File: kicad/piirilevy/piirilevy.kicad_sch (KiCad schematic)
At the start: 57 parts, among them SW1 SW_SPST, SW2 SW_Push, SW3 SW_Push, SW4 SW_Push, U1 LM324, U2 LM324, U3 LM324, U4 MAX5033B, U5 LM324, U6 uA7805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

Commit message: ...
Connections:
- net VAHVISTIN_LÄHTÖ: now also U5.13 (-), U5.14; no longer U5.1, U5.2 (-)
- net at R13.2, R14.1: now also U3.8; no longer U3.1
- net at R13.1, R8.1: now also U3.9 (-); no longer U3.2 (-)
- net at R11.2, R9.2: now also U3.10 (+); no longer U3.3 (+)
- net at R6.1: now also U2.6 (-); no longer U2.2 (-)
- net at R6.2, R7.1, R9.1: now also U2.7; no longer U2.1
- net at C4.1, R15.2: now also U5.12 (+); no longer U5.3 (+)
- net at R2.1, TH1.1: now also U2.5 (+); no longer U2.3 (+)
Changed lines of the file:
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@@
     )
   )
-  (symbol (lib_id "Amplifier_Operational:LM324") (at 73.66 74.93 0) (mirror x) (unit 1)
+  (symbol (lib_id "Amplifier_Operational:LM324") (at 73.66 74.93 0) (mirror x) (unit 3)
     (in_bom yes) (on_board yes)
     (property "Reference" "U3" (id 0) (at 73.66 80.01 0))
@@
       (effects (font (size 1.27 1.27)) hide)
     )
-    (pin "1")
-    (pin "2")
-    (pin "3")
+    (pin "10")
+    (pin "8")
+    (pin "9")
   )
   (symbol (lib_id "power:VCC") (at 194.31 111.76 0) (unit 1)
@@
     (pin "2")
   )
-  (symbol (lib_id "Amplifier_Operational:LM324") (at 111.76 72.39 0) (mirror x) (unit 1)
+  (symbol (lib_id "Amplifier_Operational:LM324") (at 111.76 72.39 0) (mirror x) (unit 4)
     (in_bom yes) (on_board yes)
     (property "Reference" "U5" (id 0) (at 111.76 77.47 0))
@@
       (effects (font (size 1.27 1.27)) hide)
     )
-    (pin "1")
-    (pin "2")
-    (pin "3")
+    (pin "12")
+    (pin "13")
+    (pin "14")
   )
   (symbol (lib_id "power:GND") (at 110.49 187.96 0) (unit 1)
@@
     (pin "1")
   )
-  (symbol (lib_id "Amplifier_Operational:LM324") (at 45.72 85.09 0) (unit 1)
+  (symbol (lib_id "Amplifier_Operational:LM324") (at 45.72 85.09 0) (unit 2)
     (in_bom yes) (on_board yes)
     (property "Reference" "U2" (id 0) (at 45.72 75.7682 0))
@@
       (effects (font (size 1.27 1.27)) hide)
     )
-    (pin "1")
-    (pin "2")
-    (pin "3")
+    (pin "5")
+    (pin "6")
+    (pin "7")
   )
   (symbol (lib_id "Device:C") (at 127 158.75 270) (unit 1)
@@
     )
     (path "/de0d0b26-5dbb-4b0b-8931-3a9405d7e432"
-      (reference "U2") (unit 1) (value "LM324") (footprint "")
+      (reference "U2") (unit 2) (value "LM324") (footprint "")
     )
     (path "/0345509e-dbff-4fb5-9059-bc7781b5488b"
-      (reference "U3") (unit 1) (value "LM324") (footprint "")
+      (reference "U3") (unit 3) (value "LM324") (footprint "")
     )
     (path "/b456cffc-d9d7-4c91-91f2-36ec9a65dd1b"
@@
     )
     (path "/d674ea40-4701-4f3e-93d0-02b0a7afdc20"
-      (reference "U5") (unit 1) (value "LM324") (footprint "")
+      (reference "U5") (unit 4) (value "LM324") (footprint "")
     )
     (path "/b3ed1808-38b3-403b-99a9-68a2b023b131"

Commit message: Muutokset piirilevyyn.
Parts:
- added C18: 22u, Capacitor_THT:C_Radial_D5.0mm_H7.0mm_P2.00mm, symbol Device:C
- added R20, R21: 4.7K, Resistor_THT:R_Axial_DIN0204_L3.6mm_D1.6mm_P7.62mm_Horizontal, symbol Device:R
- C1, C12, C13, C9: footprint (none) -> Capacitor_THT:C_Radial_D5.0mm_H7.0mm_P2.00mm
- C10, C11, C2, C3, C4, C5, C7, C8: footprint (none) -> Capacitor_THT:C_Disc_D4.3mm_W1.9mm_P5.00mm
- C14: footprint (none) -> Capacitor_THT:C_Radial_D4.0mm_H5.0mm_P1.50mm
- C15, C16, C17: footprint (none) -> Capacitor_THT:C_Rect_L7.0mm_W2.5mm_P5.00mm
- C6: footprint (none) -> Capacitor_THT:C_Radial_D10.0mm_H16.0mm_P5.00mm
- L1: footprint (none) -> Inductor_THT:L_Radial_D8.7mm_P5.00mm_Fastron_07HCP
- RV1: footprint (none) -> Potentiometer_THT:Potentiometer_ACP_CA9-H3,8_Horizontal
- TH1, V1: footprint (none) -> Connector_PinHeader_2.00mm:PinHeader_1x02_P2.00mm_Vertical
- U1: renamed from U3; footprint (none) -> Package_DIP:DIP-14_W7.62mm_LongPads
- U1: footprint Package_DIP:DIP-14_W10.16mm_LongPads -> Package_DIP:DIP-14_W7.62mm_LongPads
- U1: renamed from U5; footprint (none) -> Package_DIP:DIP-14_W7.62mm_LongPads
- U1: renamed from U2; footprint (none) -> Package_DIP:DIP-14_W7.62mm_LongPads
- U2: renamed from U6; footprint (none) -> Package_TO_SOT_THT:TO-220-3_Horizontal_TabDown
- Y1: footprint (none) -> Crystal:Crystal_HC18-U_Vertical
- renumbered U8 to U3, U7 to U5, U9 to U6
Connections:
- net GND: now also C18.1
- net I2C_SCL: now also R20.2
- net I2C_SDA: now also R21.1
- net LCD_AN: now also DS1.11 (LED(+)); no longer DS1.15 (LED(+))
- net LCD_D4: now also DS1.7 (D4); no longer DS1.11 (D4)
- net LCD_D5: now also DS1.8 (D5); no longer DS1.12 (D5)
- net LCD_D6: now also DS1.9 (D6); no longer DS1.13 (D6)
- net LCD_D7: now also DS1.10 (D7); no longer DS1.14 (D7)
- net VAHVISTIN_LÄHTÖ: now also U1.8, U1.9 (-); no longer U1.13 (-), U1.14
- net VCC: now also C18.2, R20.1, R21.2
- net at R11.2, R9.2: now also U1.5 (+); no longer U1.10 (+)
- net at R13.2, R14.1: now also U1.7; no longer U1.8
- net at R13.1, R8.1: now also U1.6 (-); no longer U1.9 (-)
- net at R19.2: now also DS1.12 (LED(-)); no longer DS1.16 (LED(-))
- net at R6.1: now also U1.13 (-); no longer U1.6 (-)
- net at R6.2, R7.1, R9.1: now also U1.14; no longer U1.7
- net at C4.1, R15.2: now also U1.10 (+); no longer U1.12 (+)
- net at R2.1, TH1.1: now also U1.12 (+); no longer U1.5 (+)

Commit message: kicad muutokset
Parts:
- added D2: 1N4148, Diode_THT:D_DO-35_SOD27_P7.62mm_Horizontal, symbol Diode:1N4148
- added J1: AVR-ISP, Connector_PinHeader_2.54mm:PinHeader_2x03_P2.54mm_Vertical, symbol Connector:AVR-ISP-6
- BZ1, SW1, SW2, SW3, SW4, TH1: footprint Connector_PinHeader_2.00mm:PinHeader_1x02_P2.00mm_Vertical -> Connector_PinHeader_2.54mm:PinHeader_1x02_P2.54mm_Vertical
- DS1: footprint Connector_PinHeader_2.00mm:PinHeader_1x12_P2.00mm_Vertical -> Connector_PinHeader_2.54mm:PinHeader_1x12_P2.54mm_Vertical
- RV1: footprint Potentiometer_THT:Potentiometer_ACP_CA9-H3,8_Horizontal -> Potentiometer_THT:Potentiometer_ACP_CA6-H2,5_Horizontal
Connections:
- net GND: now also J1.6 (GND)
- net SPI_MISO: now also J1.1 (MISO)
- net SPI_MOSI: now also J1.4 (MOSI)
- net SPI_SCK: now also J1.3 (SCK)
- net VCC: now also D2.2 (A); no longer U3.7 (VCC)
- net SW_3 renamed RESET
- net RESET: now also J1.5 (~{RST})
- new net ISP_VCC: D2.1 (K), J1.2 (VCC), U3.7 (VCC)
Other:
- moved on the sheet: C18

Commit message: Torstain muutokset.
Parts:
- removed U2: uA7805, Package_TO_SOT_THT:TO-220-3_Horizontal_TabDown, symbol Regulator_Linear:uA7805
- added U2: LM7805CV, Package_TO_SOT_THT:TO-220-3_Horizontal_TabDown, symbol Regulator_Linear:LM7805_TO220
- C1: footprint Capacitor_THT:C_Radial_D5.0mm_H7.0mm_P2.00mm -> Capacitor_THT:C_Radial_D6.3mm_H5.0mm_P2.50mm
- C12, C13: footprint Capacitor_THT:C_Radial_D5.0mm_H7.0mm_P2.00mm -> Capacitor_THT:C_Radial_D5.0mm_H5.0mm_P2.00mm
- C14: footprint Capacitor_THT:C_Radial_D4.0mm_H5.0mm_P1.50mm -> Capacitor_THT:C_Radial_D5.0mm_H5.0mm_P2.00mm
- C6: value 1m -> 330u; footprint Capacitor_THT:C_Radial_D10.0mm_H16.0mm_P5.00mm -> Capacitor_THT:C_Radial_D8.0mm_H7.0mm_P3.50mm
- C7: value 10n -> 330n
- C8: value 10n -> 100n
- L1: footprint Inductor_THT:L_Radial_D8.7mm_P5.00mm_Fastron_07HCP -> Capacitor_THT:C_Radial_D8.0mm_H7.0mm_P3.50mm
- R16: value 5M -> 820k
- R17: value 1M -> 180k
- RV1: footprint Potentiometer_THT:Potentiometer_ACP_CA6-H2,5_Horizontal -> Potentiometer_THT:Potentiometer_Vishay_T73YP_Vertical
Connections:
- net GND: now also U2.2 (GND)
- net at C7.1, R16.2, R17.1: now also U2.1 (VI)
- net at C8.1, U5.3 (CH1): now also U2.3 (VO)
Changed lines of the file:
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@@
       (effects (font (size 1.27 1.27)) (justify left))
     )
-    (property "Footprint" "Inductor_THT:L_Radial_D8.7mm_P5.00mm_Fastron_07HCP" (id 2) (at 116.84 36.83 0)
+    (property "Footprint" "Capacitor_THT:C_Radial_D8.0mm_H7.0mm_P3.50mm" (id 2) (at 116.84 36.83 0)
       (effects (font (size 1.27 1.27)) hide)
     )
@@
       (effects (font (size 1.27 1.27)) (justify left))
     )
-    (property "Footprint" "Capacitor_THT:C_Radial_D5.0mm_H7.0mm_P2.00mm" (id 2) (at 59.9948 30.48 0)
+    (property "Footprint" "Capacitor_THT:C_Radial_D6.3mm_H5.0mm_P2.50mm" (id 2) (at 59.9948 30.48 0)
       (effects (font (size 1.27 1.27)) hide)
     )
@@
       (effects (font (size 1.27 1.27)) (justify right))
     )
-    (property "Value" "10n" (id 1) (at 99.06 185.42 0)
+    (property "Value" "330n" (id 1) (at 99.06 185.42 0)
       (effects (font (size 1.27 1.27)) (justify right))
     )
@@
     (pin "1")
   )
+  (symbol (lib_id "Regulator_Linear:LM7805_TO220") (at 110.49 179.07 0) (unit 1)
+    (in_bom yes) (on_board yes)
+    (property "Reference" "U2" (id 0) (at 110.49 172.72 0))
+    (property "Value" "LM7805CV" (id 1) (at 110.49 175.26 0))
+    (property "Footprint" "Package_TO_SOT_THT:TO-220-3_Horizontal_TabDown" (id 2) (at 110.49 173.355 0)
+      (effects (font (size 1.27 1.27) italic) hide)
+    )
+    (property "Datasheet" "https://www.onsemi.cn/PowerSolutions/document/MC7800-D.PDF" (id 3) (at 110.49 180.34 0)
+      (effects (font (size 1.27 1.27)) hide)
+    )
+    (pin "1")
+    (pin "2")
+    (pin "3")
+  )
   (symbol (lib_id "Memory_NVRAM:47C16") (at 135.89 132.08 0) (unit 1)
     (in_bom yes) (on_board yes)
@@
     (property "Reference" "C12" (id 0) (at 130.81 115.5192 90))
     (property "Value" "22u" (id 1) (at 130.81 117.8306 90))
-    (property "Footprint" "Capacitor_THT:C_Radial_D5.0mm_H7.0mm_P2.00mm" (id 2) (at 127 122.8852 0)
+    (property "Footprint" "Capacitor_THT:C_Radial_D5.0mm_H5.0mm_P2.00mm" (id 2) (at 127 122.8852 0)
       (effects (font (size 1.27 1.27)) hide)
     )
@@
       (effects (font (size 1.27 1.27)) (justify left))
     )
-    (property "Value" "10n" (id 1) (at 121.92 185.42 0)
+    (property "Value" "100n" (id 1) (at 121.92 185.42 0)
       (effects (font (size 1.27 1.27)) (justify left))
     )
@@
     (property "Reference" "C13" (id 0) (at 143.51 115.5192 90))
     (property "Value" "22u" (id 1) (at 143.51 117.8306 90))
-    (property "Footprint" "Capacitor_THT:C_Radial_D5.0mm_H7.0mm_P2.00mm" (id 2) (at 139.7 122.8852 0)
+    (property "Footprint" "Capacitor_THT:C_Radial_D5.0mm_H5.0mm_P2.00mm" (id 2) (at 139.7 122.8852 0)
       (effects (font (size 1.27 1.27)) hide)
     )
@@
     )
     (pin "1")
-  )
-  (symbol (lib_id "Regulator_Linear:uA7805") (at 110.49 179.07 0) (unit 1)
-    (in_bom yes) (on_board yes)
-    (property "Reference" "U2" (id 0) (at 110.49 172.72 0))
-    (property "Value" "uA7805" (id 1) (at 110.49 175.26 0))
-    (property "Footprint" "Package_TO_SOT_THT:TO-220-3_Horizontal_TabDown" (id 2) (at 111.125 182.88 0)
-      (effects (font (size 1.27 1.27) italic) (justify left) hide)
-    )
-    (property "Datasheet" "http://www.ti.com/lit/ds/symlink/ua78.pdf" (id 3) (at 110.49 180.34 0)
-      (effects (font (size 1.27 1.27)) hide)
-    )
-    (pin "1")
-    (pin "2")
-    (pin "3")
   )
   (symbol (lib_id "Regulator_Switching:MAX5035AUPA") (at 96.52 31.75 0) (unit 1)
@@
     (in_bom yes) (on_board yes) (fields_autoplaced)
     (property "Reference" "R16" (id 0) (at 87.63 172.72 90))
-    (property "Value" "5M" (id 1) (at 87.63 175.26 90))
+    (property "Value" "820k" (id 1) (at 87.63 175.26 90))
     (property "Footprint" "Resistor_THT:R_Axial_DIN0204_L3.6mm_D1.6mm_P7.62mm_Horizontal" (id 2) (at 87.63 180.848 90)
       (effects (font (size 1.27 1.27)) hide)
@@
       (effects (font (size 1.27 1.27)) (justify left))
     )
-    (property "Value" "1m" (id 1) (at 119.761 48.133 0)
-      (effects (font (size 1.27 1.27)) (justify left))
-    )
-    (property "Footprint" "Capacitor_THT:C_Radial_D10.0mm_H16.0mm_P5.00mm" (id 2) (at 117.8052 50.8 0)
+    (property "Value" "330u" (id 1) (at 119.761 48.133 0)
+      (effects (font (size 1.27 1.27)) (justify left))
+    )
+    (property "Footprint" "Capacitor_THT:C_Radial_D8.0mm_H7.0mm_P3.50mm" (id 2) (at 117.8052 50.8 0)
       (effects (font (size 1.27 1.27)) hide)
     )
@@
     (property "Reference" "C14" (id 0) (at 95.25 99.0092 90))
     (property "Value" "1u" (id 1) (at 95.25 101.3206 90))
-    (property "Footprint" "Capacitor_THT:C_Radial_D4.0mm_H5.0mm_P1.50mm" (id 2) (at 99.06 104.4448 0)
+    (property "Footprint" "Capacitor_THT:C_Radial_D5.0mm_H5.0mm_P2.00mm" (id 2) (at 99.06 104.4448 0)
       (effects (font (size 1.27 1.27)) hide)
     )
@@
       (effects (font (size 1.27 1.27)) (justify right))
     )
-    (property "Value" "1M" (id 1) (at 90.17 185.4199 0)
+    (property "Value" "180k" (id 1) (at 90.17 185.4199 0)
       (effects (font (size 1.27 1.27)) (justify right))
     )
@@
     (property "Reference" "RV1" (id 0) (at 199.39 106.68 90))
     (property "Value" "10k" (id 1) (at 199.39 109.22 90))
-    (property "Footprint" "Potentiometer_THT:Potentiometer_ACP_CA6-H2,5_Horizontal" (id 2) (at 199.39 113.03 0)
+    (property "Footprint" "Potentiometer_THT:Potentiometer_Vishay_T73YP_Vertical" (id 2) (at 199.39 113.03 0)
       (effects (font (size 1.27 1.27)) hide)
     )
@@
     )
     (path "/3fa05934-8ad1-40a9-af5c-98ad298eb412"
-      (reference "C1") (unit 1) (value "47u") (footprint "Capacitor_THT:C_Radial_D5.0mm_H7.0mm_P2.00mm")
+      (reference "C1") (unit 1) (value "47u") (footprint "Capacitor_THT:C_Radial_D6.3mm_H5.0mm_P2.50mm")
     )
     (path "/ea4f0afc-785b-40cf-8ef1-cbe20404c18b"
@@
     )
     (path "/d1c19c11-0a13-4237-b6b4-fb2ef1db7c6d"
-      (reference "C6") (unit 1) (value "1m") (footprint "Capacitor_THT:C_Radial_D10.0mm_H16.0mm_P5.00mm")
+      (reference "C6") (unit 1) (value "330u") (footprint "Capacitor_THT:C_Radial_D8.0mm_H7.0mm_P3.50mm")
     )
     (path "/572fd832-043a-4479-ba66-950e4cf186a4"
-      (reference "C7") (unit 1) (value "10n") (footprint "Capacitor_THT:C_Disc_D4.3mm_W1.9mm_P5.00mm")
+      (reference "C7") (unit 1) (value "330n") (footprint "Capacitor_THT:C_Disc_D4.3mm_W1.9mm_P5.00mm")
     )
     (path "/9586f0dd-0000-4b42-abee-c69f7c7df23b"
-      (reference "C8") (unit 1) (value "10n") (footprint "Capacitor_THT:C_Disc_D4.3mm_W1.9mm_P5.00mm")
+      (reference "C8") (unit 1) (value "100n") (footprint "Capacitor_THT:C_Disc_D4.3mm_W1.9mm_P5.00mm")
     )
     (path "/de4bd0e7-1d23-43d7-aaa4-a8df3b9080a1"
@@
     )
     (path "/8f616ce0-61aa-4dde-a2cd-cb09a93b5a82"
-      (reference "C12") (unit 1) (value "22u") (footprint "Capacitor_THT:C_Radial_D5.0mm_H7.0mm_P2.00mm")
+      (reference "C12") (unit 1) (value "22u") (footprint "Capacitor_THT:C_Radial_D5.0mm_H5.0mm_P2.00mm")
     )
     (path "/a6c5e7f6-9bfd-4ea1-88f2-12abf15c43f3"
-      (reference "C13") (unit 1) (value "22u") (footprint "Capacitor_THT:C_Radial_D5.0mm_H7.0mm_P2.00mm")
+      (reference "C13") (unit 1) (value "22u") (footprint "Capacitor_THT:C_Radial_D5.0mm_H5.0mm_P2.00mm")
     )
     (path "/dfa9d16e-b764-4909-bfa8-e9e8bb5e3046"
-      (reference "C14") (unit 1) (value "1u") (footprint "Capacitor_THT:C_Radial_D4.0mm_H5.0mm_P1.50mm")
+      (reference "C14") (unit 1) (value "1u") (footprint "Capacitor_THT:C_Radial_D5.0mm_H5.0mm_P2.00mm")
     )
     (path "/0acc56b2-06ae-463f-8585-f554732c8061"
@@
     )
     (path "/2102c637-9f11-48f1-aae6-b4139dc22be2"
-      (reference "L1") (unit 1) (value "220u") (footprint "Inductor_THT:L_Radial_D8.7mm_P5.00mm_Fastron_07HCP")
+      (reference "L1") (unit 1) (value "220u") (footprint "Capacitor_THT:C_Radial_D8.0mm_H7.0mm_P3.50mm")
     )
     (path "/1bd8bbf7-ab8a-476a-a905-5c29b1fb5cc3"
@@
     )
     (path "/c75ec281-fee8-4545-8116-e633fc4de5bf"
-      (reference "R16") (unit 1) (value "5M") (footprint "Resistor_THT:R_Axial_DIN0204_L3.6mm_D1.6mm_P7.62mm_Horizontal")
+      (reference "R16") (unit 1) (value "820k") (footprint "Resistor_THT:R_Axial_DIN0204_L3.6mm_D1.6mm_P7.62mm_Horizontal")
     )
     (path "/e39d87c5-11aa-4fb2-9237-1672c4a56c7d"
-      (reference "R17") (unit 1) (value "1M") (footprint "Resistor_THT:R_Axial_DIN0204_L3.6mm_D1.6mm_P7.62mm_Horizontal")
+      (reference "R17") (unit 1) (value "180k") (footprint "Resistor_THT:R_Axial_DIN0204_L3.6mm_D1.6mm_P7.62mm_Horizontal")
     )
     (path "/b6b0213a-7a3f-499b-b9b4-dac6c495ac86"
@@
     )
     (path "/f477e48c-ee20-474b-b17e-bd5e976db4c5"
-      (reference "RV1") (unit 1) (value "10k") (footprint "Potentiometer_THT:Potentiometer_ACP_CA6-H2,5_Horizontal")
+      (reference "RV1") (unit 1) (value "10k") (footprint "Potentiometer_THT:Potentiometer_Vishay_T73YP_Vertical")
     )
     (path "/ea28e946-b74f-4ba8-ac7b-b1884c5e7296"
@@
       (reference "U1") (unit 4) (value "LM324") (footprint "Package_DIP:DIP-14_W7.62mm_LongPads")
     )
-    (path "/b3ed1808-38b3-403b-99a9-68a2b023b131"
-      (reference "U2") (unit 1) (value "uA7805") (footprint "Package_TO_SOT_THT:TO-220-3_Horizontal_TabDown")
+    (path "/83d289e8-09e9-450f-aa29-e4a965c20aed"
+      (reference "U2") (unit 1) (value "LM7805CV") (footprint "Package_TO_SOT_THT:TO-220-3_Horizontal_TabDown")
     )
     (path "/7777dc6e-3b73-4e0a-9057-01bbcecb3cce"

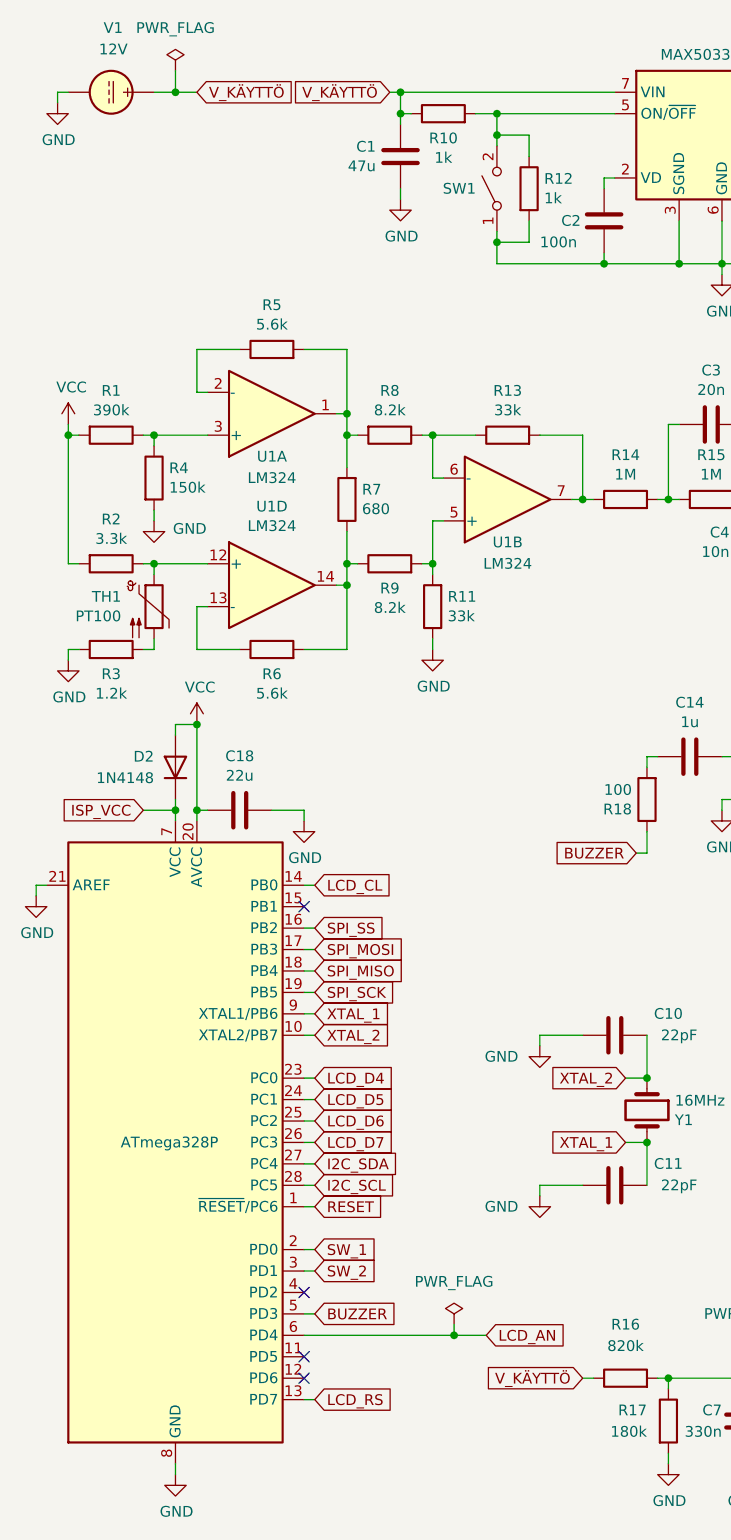
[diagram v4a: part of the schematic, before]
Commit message: Korjaukset piirilevyyn + CNC tiedostot ja kuvat.
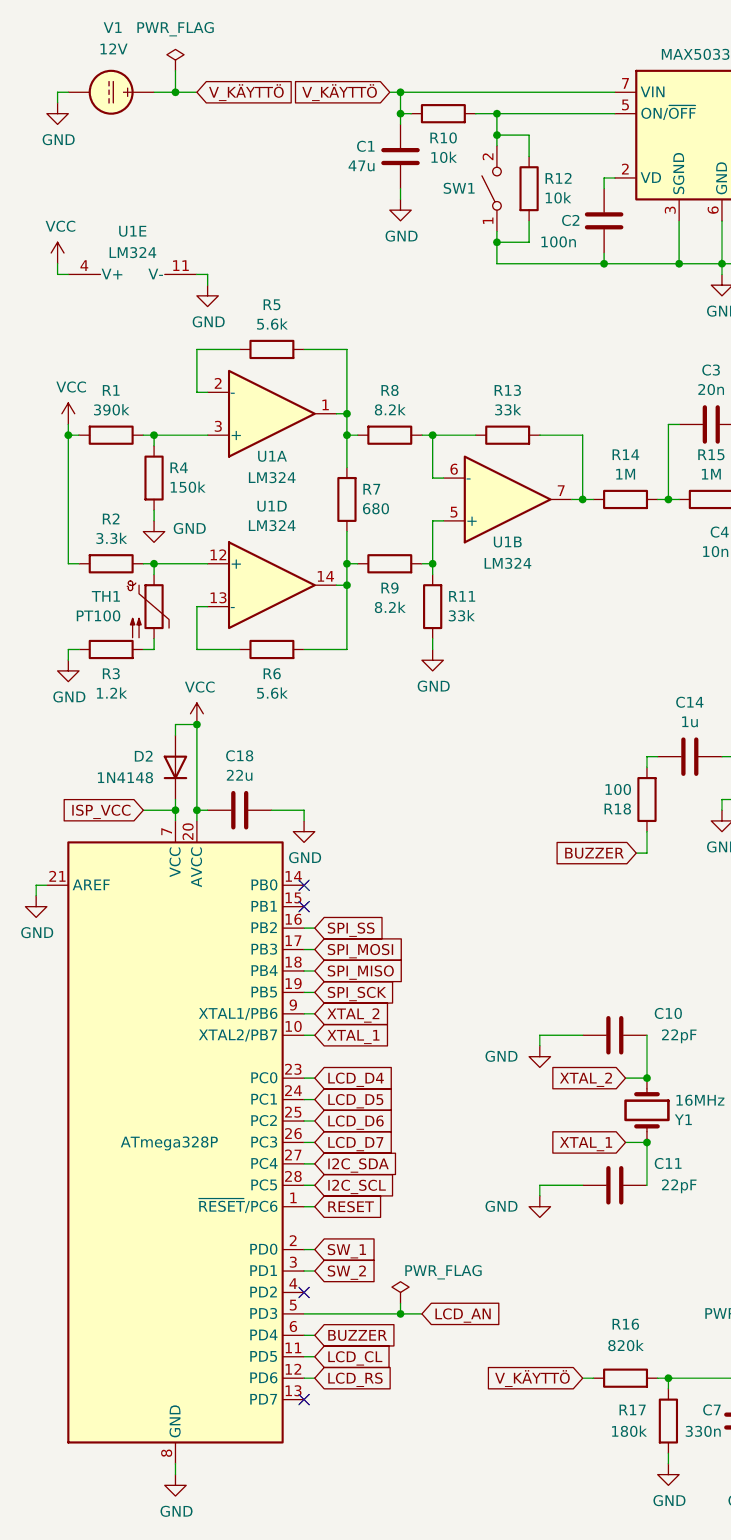
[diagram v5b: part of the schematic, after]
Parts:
- added unit 5 of U1
- C15, C16, C17: footprint Capacitor_THT:C_Rect_L7.0mm_W2.5mm_P5.00mm -> Capacitor_THT:C_Disc_D4.3mm_W1.9mm_P5.00mm
- R10, R12: value 1k -> 10k
- V1: footprint Connector_PinHeader_2.00mm:PinHeader_1x02_P2.00mm_Vertical -> Connector_PinHeader_2.54mm:PinHeader_1x02_P2.54mm_Vertical
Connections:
- net BUZZER: now also U3.6 (PD4); no longer U3.5 (PD3)
- net GND: now also U1.11 (V-)
- net LCD_AN: now also U3.5 (PD3); no longer U3.6 (PD4)
- net LCD_CL: now also U3.11 (PD5); no longer U3.14 (PB0)
- net LCD_RS: now also U3.12 (PD6); no longer U3.13 (PD7)
- net VCC: now also U1.4 (V+)
- net XTAL_1: now also U3.10 (XTAL2/PB7); no longer U3.9 (XTAL1/PB6)
- net XTAL_2: now also U3.9 (XTAL1/PB6); no longer U3.10 (XTAL2/PB7)
